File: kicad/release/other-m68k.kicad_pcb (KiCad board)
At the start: 4 copper layers, 180 x 125 mm, 146 parts, among them J1 USB-C power, J2 FTDI (GND CTS VCC TXD RXD RTS), J3 PS/2, J4 microSD DM3AT-SF-PEJM5, J5 RCA composite, J6 3.5mm audio, J7 JTAG (ByteBlaster), J8 Expansion, J9 Logic analyzer (gusmanb 2x15), SW1 RESET, SW2 NMI, U1 MC68000P12, U10 MC68681P, U11 AD724JR, U12 AP2112K-3.3, U13 MCP130T-450I/TT, U2 AS6C4008-55PCN (upper, D15..D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, U3 AS6C4008-55PCN (lower, D7..D0), U4 SST39SF040-70 (even, D15..D8), U5 SST39SF040-70 (odd, D7..D0), U6 ATF1508AS-7JX84 (MMU), U7 ATF1508AS-7JX84 (I/O), U8 74AHCT245 (hi), U9 74AHCT245 (lo), X1 24MHz, Y1 3.6864MHz, Y2 3.579545MHz

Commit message: rev C1: audio low-pass 33 nF (C31); sys_read may fill a held BIOS audio buffer
Board: the 1 k / 10 nF low-pass (16 kHz corner, which passed the PDM sigma-delta hiss above
8 kHz) becomes 1 k / 33 nF (4.8 kHz). Same 0603 footprint and nets, so the routed board is
unchanged except C31's value: fab package and release snapshot regenerated from it (DRC 0,
0 unrouted). parts.json: Samsung CL10B333KB8NFNC, LCSC C307488. In the emulator
reconstruction of the tune example the power above 8 kHz relative to the music band drops
from -14 dB to -20.5 dB. ORDER.md names the B4 hand change.

Firmware (spec rev 8 wording): sys_read accepts a destination inside the BIOS audio buffers
while a stream is open (audio_buf_range_ok), so a file streams straight into the buffer the
program holds; sdplay reads raw PDM that way instead of copying. Host tests 401.

Co-Authored-By: Claude Fable 5.1 <noreply@anthropic.com>
Claude-Session: https://claude.ai/code/session_019bbFLKMxhKXGW6aABP44Z1
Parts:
- C31: value 10nF -> 33nF
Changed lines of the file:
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@@
 			)
 		)
-		(property "Value" "10nF"
+		(property "Value" "33nF"
 			(at 0 1.43 90)
 			(layer "F.Fab")

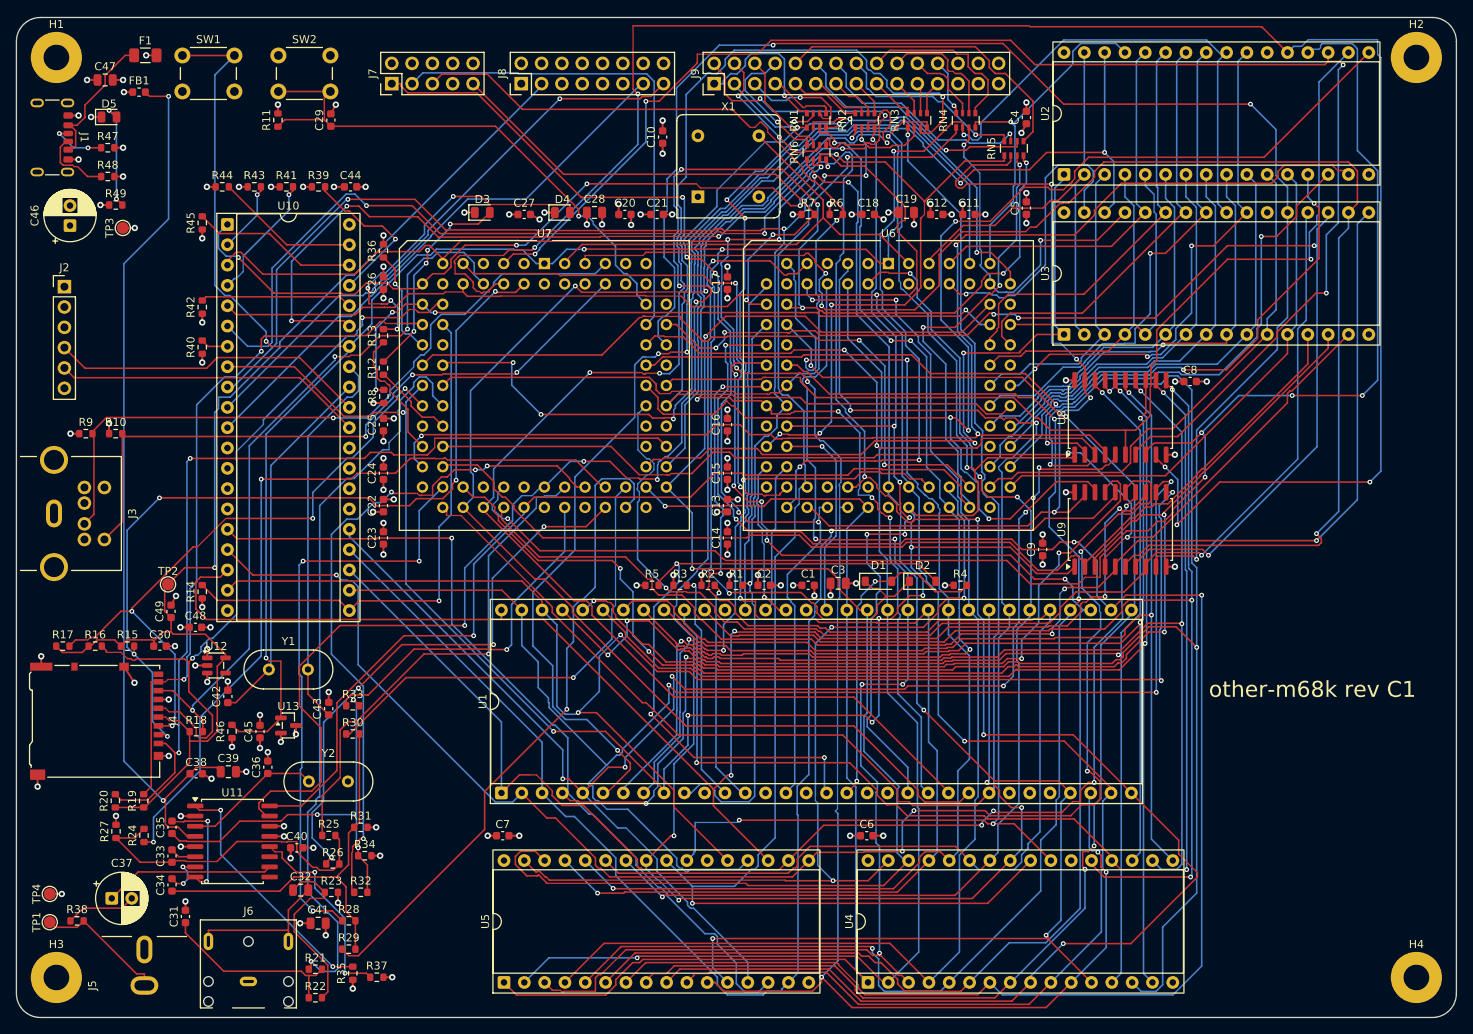
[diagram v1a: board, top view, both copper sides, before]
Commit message: board rev C2 (spec rev 10): front and back edges, S-video jack, serial B header, dedication silkscreen
The rev B4 order was stopped; rev C2 is what goes to PCBWay. The sheet's bottom edge is the
machine's front: J3 PS/2, J6 audio, J4 microSD (LDO behind it), then SW1 RESET and SW2 NMI
with the LEDs D5 PWR, D3 LED0, D4 LED1 behind them, all labelled. The top edge is the back:
J1 USB-C, J2 serial A, J11 serial B (a second FTDI-pinout header on DUART channel B; it
replaces the 2x8 expansion header J8, which carried only channel B and the rails after spec
rev 7), J5 composite, J10 S-video (CUI MD-40SM mini-DIN 4 on the AD724's LUMA and CRMA
outputs through 220 uF and 75 ohm each; new footprint and symbol in kicad/lib). J9 (logic
analyzer) and J7 (JTAG) stand on the left edge with the six series arrays hand-placed in a
spaced column (the auto-placed cluster left one connection unroutable). The flash chips
stand vertically at the right edge; the AD724 section sits right of the S-video jack; the
bus buffers moved under the SRAMs. The open area under the CPU carries "Griffin Jr.",
"October 2026", "I love you, Kris!" and the revision; connector labels are placed where
the silkscreen checker finds them free of pads and other silk.

Routed by freerouting (optimizer on): 0 DRC violations, 0 unrouted. Fab package and
release regenerated; ORDER.md rewritten for rev C2. Spec rev 10 carries only the connector
wording (serial headers, S-video); no register or firmware change.

Co-Authored-By: Claude Fable 5.1 <noreply@anthropic.com>
Claude-Session: https://claude.ai/code/session_019bbFLKMxhKXGW6aABP44Z1
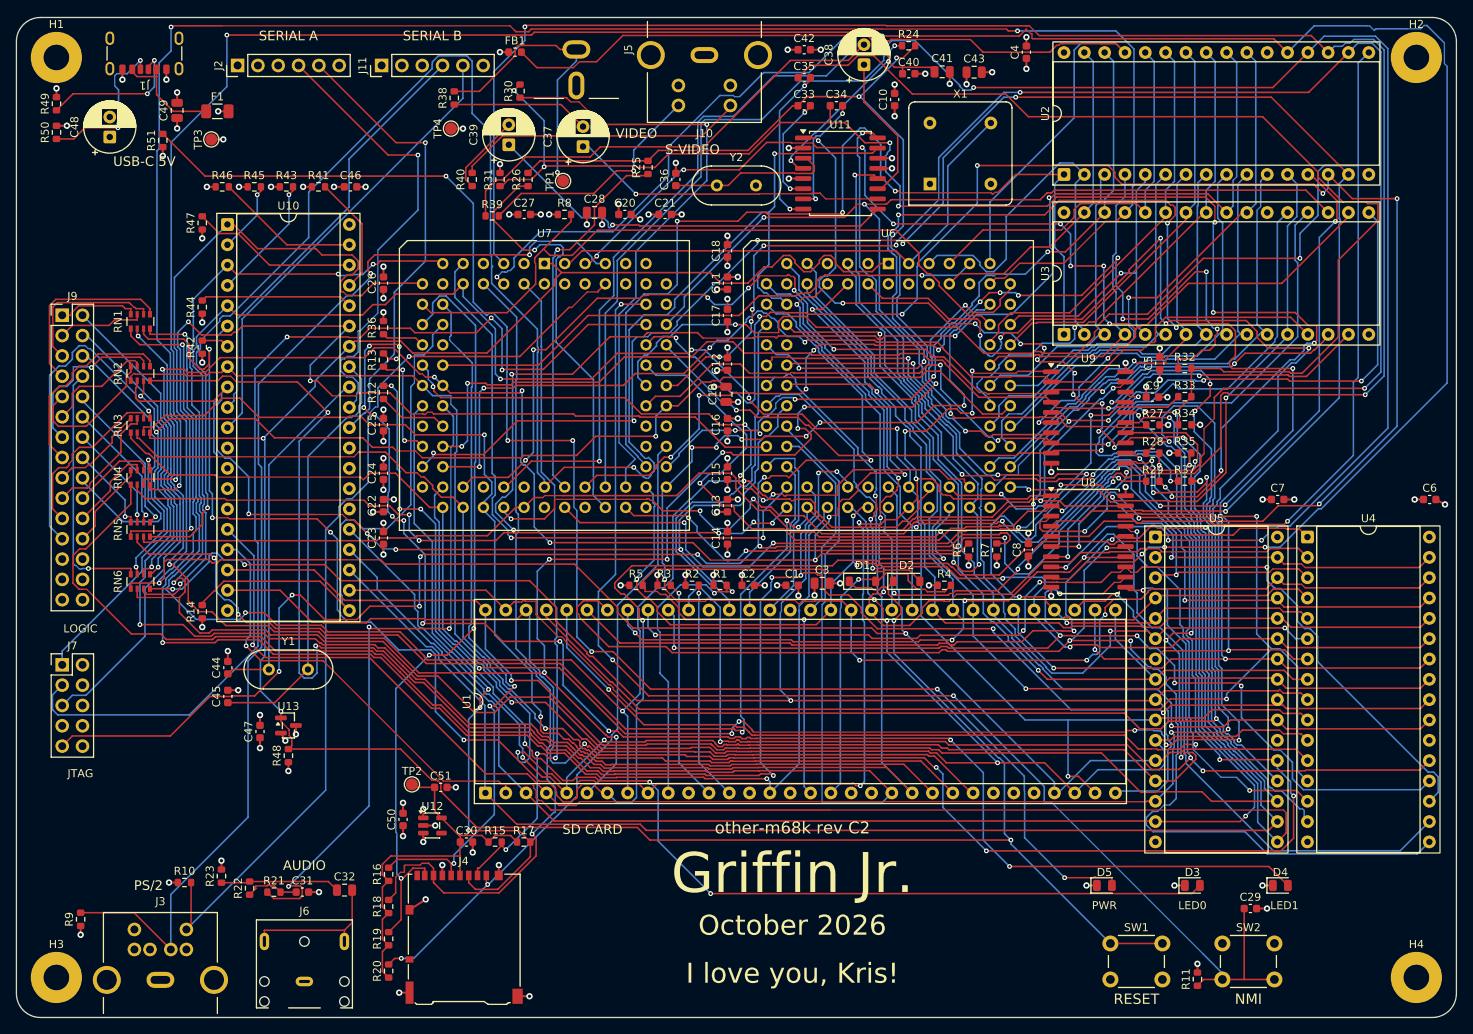
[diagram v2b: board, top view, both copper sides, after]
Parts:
- removed J8: Expansion, PinHeader_2x08_P2.54mm_Vertical
- added C50: 1uF, C_0603_1608Metric, F.Cu at (48.3, 100.2)
- added C51: 1uF, C_0603_1608Metric, F.Cu at (53.0, 96.2)
- added J10: S-video, MiniDIN-4_CUI_MD-40SM_Horizontal, F.Cu at (86.0, 0.00)
- added J11: FTDI B (GND CTS VCC TXD RXD RTS), PinHeader_1x06_P2.54mm_Vertical, F.Cu at (45.6, 6.00)
- added R50: 5.1k, R_0603_1608Metric, F.Cu at (5.01, 14.4)
- added R51: 1k, R_0603_1608Metric, F.Cu at (18.3, 15.4)
- C38: value 100nF -> 220uF; footprint C_0603_1608Metric -> CP_Radial_D6.3mm_P2.50mm
- C39: value 10uF -> 220uF; footprint C_0805_2012Metric -> CP_Radial_D6.3mm_P2.50mm
- C42: value 15pF -> 100nF
- C43: value DNP (0-5pF) -> 10uF; footprint C_0603_1608Metric -> C_0805_2012Metric
- C44: value 100nF -> 15pF
- C45: value 100nF -> DNP (0-5pF)
- C46: value 100uF -> 100nF; footprint CP_Radial_D6.3mm_P2.50mm -> C_0603_1608Metric
- C47: value 10uF -> 100nF; footprint C_0805_2012Metric -> C_0603_1608Metric
- C48: value 1uF -> 100uF; footprint C_0603_1608Metric -> CP_Radial_D6.3mm_P2.50mm
- C49: value 1uF -> 10uF; footprint C_0603_1608Metric -> C_0805_2012Metric
- R39: value 4.7k -> 75
- R40: value 10k -> 75
- R41: value 10k -> 4.7k
- R47, R48: value 5.1k -> 10k
- R49: value 1k -> 5.1k
- moved SW2 162.0 mm to (150.8, 115.8)
- moved SW1 160.6 mm to (136.8, 115.8)
- moved R11 157.3 mm to (147.6, 120.2)
- moved D5 157.2 mm to (136.0, 108.5)
- moved C29 151.4 mm to (154.2, 111.4), turned to 0 degrees
- moved R27 139.2 mm to (142.1, 50.9), turned to 0 degrees
- moved R24 137.4 mm to (111.5, 3.53), turned to 0 degrees
- moved J5 136.2 mm to (70.0, 0.00), turned to -90 degrees
- moved C41 132.0 mm to (115.7, 6.79)
- moved C34 128.0 mm to (102.5, 11.0), turned to 0 degrees
- moved C40 123.3 mm to (111.5, 7.03)
- moved D4 123.0 mm to (158.0, 108.5)
- moved R35 122.7 mm to (146.1, 54.4), turned to 0 degrees
- moved C33 122.6 mm to (98.5, 11.0), turned to 0 degrees
- moved C35 122.6 mm to (98.5, 7.53), turned to 0 degrees
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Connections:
- C38 pad 1: +5VA -> LUMA
- C38 pad 2: GND -> LUMA_AC
- C39 pad 1: +5VA -> CRMA
- C39 pad 2: GND -> CRMA_AC
- C40 pad 1: VCC -> +5VA
- C41 pad 1: VCC -> +5VA
- C42 pad 1: DUART_X1 -> VCC
- C43 pad 1: DUART_X2 -> VCC
- C44 pad 1: VCC -> DUART_X1
- C45 pad 1: VCC -> DUART_X2
- C49 pad 1: +3V3 -> VCC
- R39 pad 1: VCC -> LUMA_AC
- R39 pad 2: DUART_IACK -> SVIDEO_Y
- R40 pad 1: VCC -> CRMA_AC
- R40 pad 2: DUART_IP0 -> SVIDEO_C
- R41 pad 2: DUART_IP1 -> DUART_IACK
- R42 pad 2: DUART_IP2 -> DUART_IP0
- R43 pad 2: DUART_IP3 -> DUART_IP1
- R44 pad 2: DUART_IP4 -> DUART_IP2
- R45 pad 2: DUART_IP5 -> DUART_IP3
- R46 pad 2: SYSRESET -> DUART_IP4
- R47 pad 1: CC1 -> VCC
- R47 pad 2: GND -> DUART_IP5
- R48 pad 1: CC2 -> VCC
- R48 pad 2: GND -> SYSRESET
- R49 pad 1: VCC -> CC1
- R49 pad 2: PWRLED_A -> GND
- U10 pad 10: DUART_RXDB -> FTDIB_TXD
- U10 pad 11: DUART_TXDB -> FTDIB_RXD
- U11 pad 11: unconnected-(U11-LUM_OUT-Pad11) -> LUMA
- U11 pad 9: unconnected-(U11-CHROM_OUT-Pad9) -> CRMA
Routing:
- net WEL: track 44.6 -> 226.7 mm, vias 2 -> 3
- net PWRLED_A: track 13.9 -> 192.5 mm, vias 2 -> 6
- net WEU: track 43.9 -> 217.1 mm, vias 1 -> 2
- net LED1_A: track 42.8 -> 176.7 mm, vias 4 -> 12
- net G_DAC: track 50.4 -> 182.7 mm, vias 0 -> 11
- net LED0_A: track 26.2 -> 151.3 mm, vias 4 -> 6
- net JTAG_TDI: track 68.1 -> 193.1 mm, vias 2 -> 8
- net G2: track 73.9 -> 183.8 mm, vias 3 -> 7
- net RAMOE: track 134.8 -> 237.5 mm, vias 4 -> 9
- net +3V3: track 151.2 -> 50.1 mm, vias 1 -> 0
- net VPA: track 107.9 -> 204.3 mm, vias 6 -> 2
- net NMIBTN: track 68.8 -> 162.6 mm, vias 1 -> 3
- net R_DAC: track 40.7 -> 127.1 mm, vias 0 -> 3
- net JTAG_TMS: track 131.9 -> 216.8 mm, vias 1 -> 8
- net MD12: track 129.7 -> 212.9 mm, vias 1 -> 9
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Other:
- board text added: "AUDIO"
- board text added: "Griffin Jr."
- board text added: "I love you, Kris!"
- board text added: "JTAG"
- board text added: "LED0"
- board text added: "LED1"
- board text added: "LOGIC"
- board text added: "NMI"
- board text added: "October 2026"
- board text added: "PS/2"
- board text added: "PWR"
- board text added: "RESET"
- board text added: "S-VIDEO"
- board text added: "SD CARD"
- board text added: "SERIAL A"
- board text added: "SERIAL B"
- board text added: "USB-C 5V"
- board text added: "VIDEO"
- board text added: "other-m68k rev C2"
- board text removed: "other-m68k rev C1"
